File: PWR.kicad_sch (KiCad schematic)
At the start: 3 parts

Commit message: PCB drawn
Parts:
- C32, C33: value (none) -> 100n; footprint (none) -> Capacitor_SMD:C_0603_1608Metric
- U11: value (none) -> HX9193; footprint (none) -> Package_TO_SOT_SMD:SOT-23-5_HandSoldering
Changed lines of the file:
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@@
     (in_bom yes) (on_board yes) (fields_autoplaced)
     (property "Reference" "U11" (id 0) (at 146.685 69.8205 0))
-    (property "Value" "" (id 1) (at 146.685 72.5956 0))
-    (property "Footprint" "" (id 2) (at 147.32 80.01 0)
+    (property "Value" "HX9193" (id 1) (at 146.685 72.5956 0))
+    (property "Footprint" "Package_TO_SOT_SMD:SOT-23-5_HandSoldering" (id 2) (at 147.32 80.01 0)
       (effects (font (size 1.27 1.27)) hide)
     )
@@
   (symbol (lib_id "power:GND") (at 160.02 87.63 0) (unit 1)
     (in_bom yes) (on_board yes) (fields_autoplaced)
-    (property "Reference" "#PWR?" (id 0) (at 160.02 93.98 0)
+    (property "Reference" "#PWR0105" (id 0) (at 160.02 93.98 0)
       (effects (font (size 1.27 1.27)) hide)
     )
-    (property "Value" "" (id 1) (at 160.02 92.1925 0))
+    (property "Value" "GND" (id 1) (at 160.02 92.1925 0))
     (property "Footprint" "" (id 2) (at 160.02 87.63 0)
       (effects (font (size 1.27 1.27)) hide)
@@
       (effects (font (size 1.27 1.27)) (justify right))
     )
-    (property "Value" "" (id 1) (at 134.112 79.502 0)
+    (property "Value" "100n" (id 1) (at 134.112 79.502 0)
       (effects (font (size 1.27 1.27)) (justify right))
     )
-    (property "Footprint" "" (id 2) (at 134.62 77.47 0)
+    (property "Footprint" "Capacitor_SMD:C_0603_1608Metric" (id 2) (at 134.62 77.47 0)
       (effects (font (size 1.27 1.27)) hide)
     )
@@
       (effects (font (size 1.27 1.27)) (justify right))
     )
-    (property "Value" "" (id 1) (at 160.528 83.312 0)
+    (property "Value" "100n" (id 1) (at 160.528 83.312 0)
       (effects (font (size 1.27 1.27)) (justify right))
     )
-    (property "Footprint" "" (id 2) (at 160.02 81.28 0)
+    (property "Footprint" "Capacitor_SMD:C_0603_1608Metric" (id 2) (at 160.02 81.28 0)
       (effects (font (size 1.27 1.27)) hide)
     )
@@
   (symbol (lib_id "power:GND") (at 134.62 86.36 0) (unit 1)
     (in_bom yes) (on_board yes) (fields_autoplaced)
-    (property "Reference" "#PWR?" (id 0) (at 134.62 92.71 0)
+    (property "Reference" "#PWR0104" (id 0) (at 134.62 92.71 0)
       (effects (font (size 1.27 1.27)) hide)
     )
-    (property "Value" "" (id 1) (at 134.62 90.9225 0))
+    (property "Value" "GND" (id 1) (at 134.62 90.9225 0))
     (property "Footprint" "" (id 2) (at 134.62 86.36 0)
       (effects (font (size 1.27 1.27)) hide)

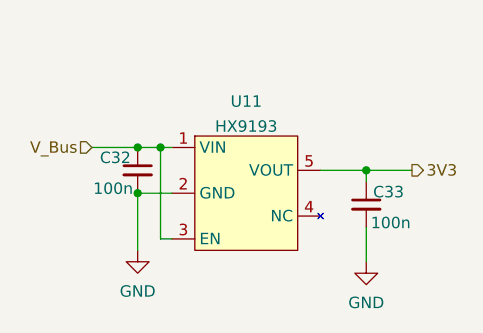
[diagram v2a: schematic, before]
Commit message: Add ESD protection
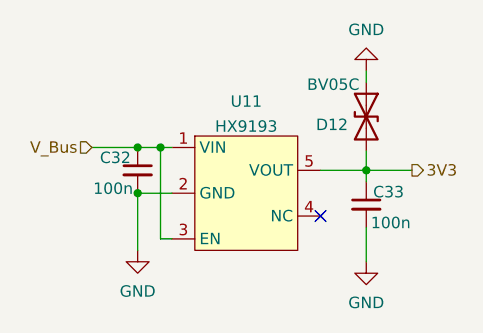
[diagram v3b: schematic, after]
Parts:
- added D12: BV05C, Diode_SMD:D_SOD-323, symbol Device:D_TVS
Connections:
- net 3V3: now also D12.2 (A2)
- net GND: now also D12.1 (A1)
- no-connect marks 0 -> 1
